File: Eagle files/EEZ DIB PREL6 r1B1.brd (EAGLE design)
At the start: 146 x 95 mm, 66 parts, among them IC1 STM32F030C6T6, IC2 74HC1G126DBVT, IC3 M24C32-WMN6P, IC4 LP2985-33DBVR, K1 RT424005, K2 RT424005, K3 RT424005, K4 RT424005, K5 RT424005, K6 RT424005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

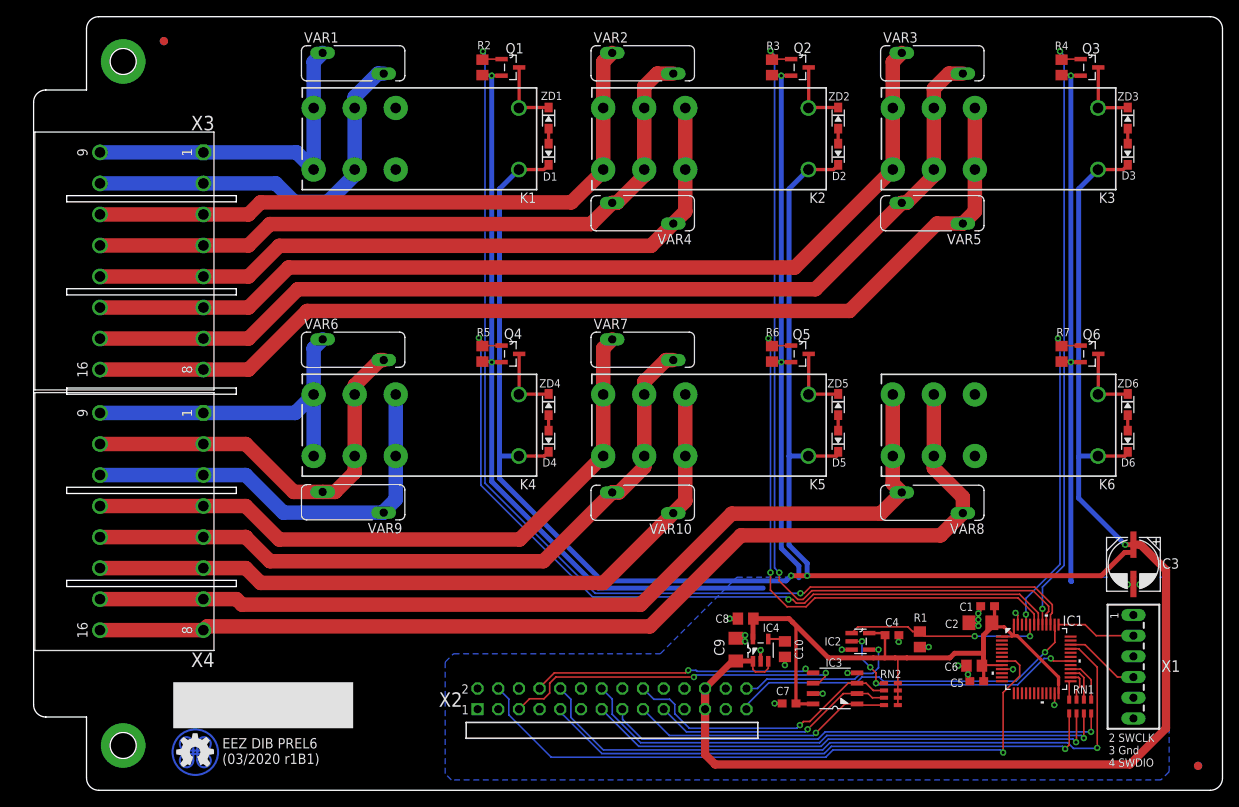
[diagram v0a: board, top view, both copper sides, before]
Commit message: BOM added, improved PCB clearances
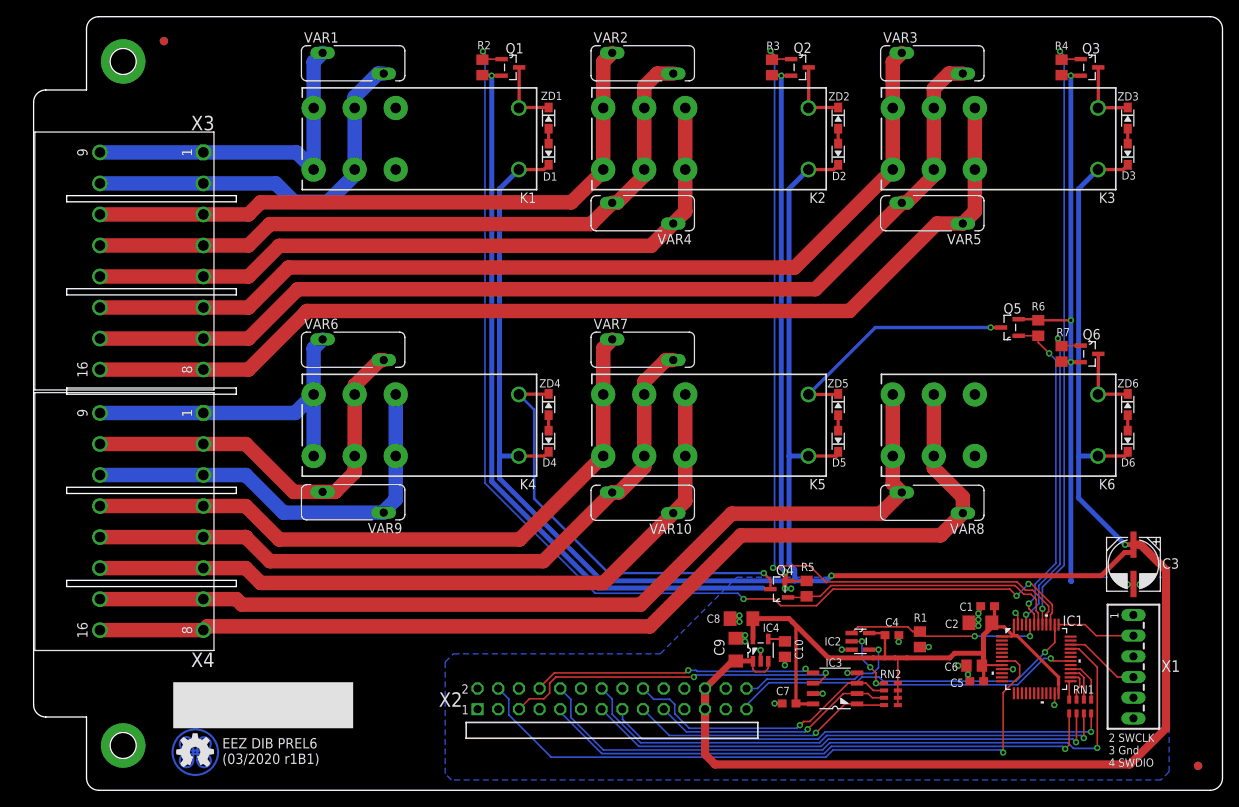
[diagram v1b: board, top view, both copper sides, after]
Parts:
- C8: device rcl:C0805 -> rcl:C1206
- moved R5 49.2 mm to (94.9, 24.8), turned to 90 degrees
- moved Q4 43.9 mm to (91.6, 24.7), turned to 180 degrees
- moved R6 32.9 mm to (123.4, 56.8), turned to 90 degrees
- moved Q5 26.0 mm to (119.9, 56.8), turned to 180 degrees
- moved C8 0.51 mm to (86.9, 21.1)
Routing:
- net PREL3: track 99.0 -> 35.0 mm, vias 2 -> 0
- net N$9: track 8.63 -> 51.5 mm, vias 0 -> 1
- net PREL4: track 70.3 -> 40.4 mm
- net N$11: track 8.63 -> 30.7 mm, vias 0 -> 1
- net GND: track 248.1 -> 253.5 mm, vias 27 -> 30
- net PREL0: track 135.5 -> 137.7 mm, vias 2 -> 4
- net PREL1: track 106.7 -> 105.7 mm
- net +5V: vias 3 -> 2

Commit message: UART relocated
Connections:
- removed net OUT22: IC1.2
- removed net OUT23: IC1.3
- net UART_RX: now also IC1.31; no longer IC1.38
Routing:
- net UART_RX: track 44.2 -> 43.6 mm
- net N$19: track 51.9 -> 52.5 mm
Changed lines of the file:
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@@
 <layer number="25" name="tNames" color="7" fill="1" visible="yes" active="yes"/>
 <layer number="26" name="bNames" color="5" fill="1" visible="no" active="yes"/>
-<layer number="27" name="tValues" color="14" fill="1" visible="yes" active="yes"/>
+<layer number="27" name="tValues" color="14" fill="1" visible="no" active="yes"/>
 <layer number="28" name="bValues" color="10" fill="1" visible="no" active="yes"/>
 <layer number="29" name="tStop" color="7" fill="1" visible="yes" active="yes"/>
@@
 <via x="86.6775" y="20.701" extent="1-16" drill="0.4" shape="square"/>
 </signal>
-<signal name="OUT23">
-<contactref element="IC1" pad="3"/>
-</signal>
-<signal name="OUT22">
-<contactref element="IC1" pad="2"/>
-</signal>
 <signal name="DIB_A0">
 <contactref element="IC3" pad="1"/>
@@
 <contactref element="RN2" pad="1"/>
 <contactref element="IC2" pad="2"/>
-<via x="124.9045" y="16.1925" extent="1-16" drill="0.4" shape="octagon"/>
+<via x="125.095" y="15.875" extent="1-16" drill="0.4" shape="octagon"/>
 <wire x1="104.433" y1="13.161" x2="104.22" y2="13.161" width="0.2032" layer="1"/>
 <via x="102.743" y="15.113" extent="1-16" drill="0.4" shape="octagon"/>
@@
 <wire x1="103.4415" y1="13.1445" x2="103.4415" y2="14.4145" width="0.2032" layer="1"/>
 <wire x1="103.4415" y1="14.4145" x2="102.743" y2="15.113" width="0.2032" layer="1"/>
-<wire x1="127.3429" y1="15.875" x2="125.222" y2="15.875" width="0.2032" layer="1"/>
-<wire x1="125.222" y1="15.875" x2="124.9045" y2="16.1925" width="0.2032" layer="1"/>
-<wire x1="124.9045" y1="16.1925" x2="124.079" y2="16.1925" width="0.2032" layer="16"/>
-<wire x1="124.079" y1="16.1925" x2="120.8405" y2="12.954" width="0.2032" layer="16"/>
-<wire x1="120.8405" y1="12.954" x2="103.632" y2="12.954" width="0.2032" layer="16"/>
+<wire x1="127.3429" y1="15.875" x2="125.095" y2="15.875" width="0.2032" layer="1"/>
+<wire x1="123.825" y1="15.875" x2="120.904" y2="12.954" width="0.2032" layer="16"/>
+<wire x1="120.904" y1="12.954" x2="103.632" y2="12.954" width="0.2032" layer="16"/>
 <wire x1="103.632" y1="12.954" x2="103.4415" y2="13.1445" width="0.2032" layer="16"/>
+<wire x1="125.095" y1="15.875" x2="123.825" y2="15.875" width="0.2032" layer="16"/>
 </signal>
 <signal name="SWDIO">
@@
 </signal>
 <signal name="UART_RX">
-<contactref element="IC1" pad="38"/>
 <contactref element="X2" pad="27"/>
-<wire x1="125.3871" y1="20.3454" x2="125.3871" y2="19.5834" width="0.2032" layer="1"/>
-<wire x1="125.3871" y1="19.5834" x2="125.4125" y2="19.558" width="0.2032" layer="1"/>
-<wire x1="125.4125" y1="19.558" x2="125.4125" y2="18.161" width="0.2032" layer="1"/>
-<via x="124.206" y="16.9545" extent="1-16" drill="0.4" shape="octagon"/>
+<via x="124.587" y="16.891" extent="1-16" drill="0.4" shape="octagon"/>
 <wire x1="87.54" y1="9.96" x2="87.54" y2="10.451" width="0.2032" layer="16"/>
 <wire x1="87.54" y1="10.451" x2="90.297" y2="13.208" width="0.2032" layer="16"/>
@@
 <wire x1="101.0285" y1="13.208" x2="90.297" y2="13.208" width="0.2032" layer="16"/>
 <wire x1="101.727" y1="13.9065" x2="103.8225" y2="13.9065" width="0.2032" layer="16"/>
-<wire x1="125.4125" y1="18.161" x2="124.206" y2="16.9545" width="0.2032" layer="1"/>
 <wire x1="103.8225" y1="13.9065" x2="104.3305" y2="13.3985" width="0.2032" layer="16"/>
-<wire x1="124.206" y1="16.9545" x2="120.65" y2="13.3985" width="0.2032" layer="16"/>
-<wire x1="120.65" y1="13.3985" x2="104.3305" y2="13.3985" width="0.2032" layer="16"/>
+<wire x1="120.7135" y1="13.3985" x2="104.3305" y2="13.3985" width="0.2032" layer="16"/>
+<contactref element="IC1" pad="31"/>
+<wire x1="120.7135" y1="13.3985" x2="124.206" y2="16.891" width="0.2032" layer="16"/>
+<wire x1="124.587" y1="16.891" x2="124.206" y2="16.891" width="0.2032" layer="16"/>
+<wire x1="127.3429" y1="16.383" x2="125.603" y2="16.383" width="0.2032" layer="1"/>
+<wire x1="124.587" y1="16.891" x2="125.095" y2="16.891" width="0.2032" layer="1"/>
+<wire x1="125.095" y1="16.891" x2="125.603" y2="16.383" width="0.2032" layer="1"/>
 </signal>
 <signal name="SWCLK">
@@
 <contactref element="X4" pad="3"/>
 <contactref element="X4" pad="11"/>
-<wire x1="42.993" y1="34.0995" x2="30.6705" y2="34.0995" width="1.778" layer="16"/>
-<wire x1="30.6705" y1="34.0995" x2="26.055" y2="38.715" width="1.778" layer="16"/>
+<wire x1="31.369" y1="33.401" x2="26.055" y2="38.715" width="1.778" layer="16"/>
 <wire x1="20.85" y1="38.715" x2="26.055" y2="38.715" width="1.778" layer="16"/>
 <wire x1="42.993" y1="34.0995" x2="42.993" y2="34.23" width="1.778" layer="16"/>
@@
 <wire x1="44.47" y1="48.611" x2="44.47" y2="41.051" width="1.778" layer="16"/>
 <wire x1="8.15" y1="38.715" x2="20.85" y2="38.715" width="1.778" layer="16"/>
+<wire x1="31.369" y1="33.401" x2="42.2945" y2="33.401" width="1.778" layer="16"/>
+<wire x1="42.2945" y1="33.401" x2="42.993" y2="34.0995" width="1.778" layer="16"/>
 </signal>
 <signal name="N$22">

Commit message: debug connector update
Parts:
- X1: value N.C. -> SSW-106-02-S-S; device EEZ_connectors:22-23-2061 -> con-samtec:SSW-106-02-S-S
- moved X1 2.35 mm to (132.7, 15.2)
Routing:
- net SWCLK: track 9.76 -> 7.41 mm
- net SWDIO: track 9.37 -> 7.02 mm
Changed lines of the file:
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@@
 <rectangle x1="19.6119" y1="7.0038" x2="20.0119" y2="7.0076" layer="21"/>
 <rectangle x1="19.6652" y1="7.0076" x2="19.9052" y2="7.0114" layer="21"/>
-<text x="132.0192" y="6.9627" size="1.016" layer="21" font="vector" ratio="10" rot="SR0" align="top-left">2 SWCLK
+<text x="132.5272" y="6.9627" size="1.016" layer="21" font="vector" ratio="10" rot="SR0" align="top-left">2 SWCLK
 3 Gnd
 4 SWDIO
@@
 <attribute name="VALUE" x="96.3676" y="17.907" size="0.6096" layer="27" ratio="10" rot="SR0"/>
 </element>
-<element name="X1" library="EEZ_connectors" package="22-23-2061" value="N.C." x="135.0645" y="15.1765" smashed="yes" rot="R270">
-<attribute name="OC_NEWARK" value="27C1933" x="135.0645" y="15.1765" size="1.016" layer="27" ratio="10" rot="R270" display="off"/>
-<attribute name="MPN" value="22-23-2061" x="135.0645" y="15.1765" size="1.016" layer="27" ratio="10" rot="R270" display="off"/>
-<attribute name="MF" value="MOLEX" x="135.0645" y="15.1765" size="1.016" layer="27" ratio="10" rot="R270" display="off"/>
-<attribute name="OC_FARNELL" value="1462922" x="135.0645" y="15.1765" size="1.016" layer="27" ratio="10" rot="R270" display="off"/>
-<attribute name="NAME" x="138.4935" y="14.5415" size="1.4224" layer="25" ratio="10"/>
-<attribute name="VALUE" x="132.207" y="18.034" size="1.016" layer="27" ratio="10" rot="R270"/>
-</element>
 <element name="EEZ_SIGNATURE" library="EEZ_Lib1" package="SIGNATURE_5MM" value="SIGNATURESMALL" x="19.8585" y="4.6765" smashed="yes" rot="R180"/>
 <element name="FM2" library="EEZ_Lib1" package="FIDUCIAL_DUAL" value="FIDUCIAL_2" x="143" y="3" smashed="yes"/>
@@
 <attribute name="NAME" x="125.603" y="55.753" size="1.016" layer="25" ratio="10"/>
 <attribute name="VALUE" x="126.238" y="53.594" size="1.016" layer="27" ratio="10" rot="R270" align="center"/>
+</element>
+<element name="X1" library="con-samtec" package="SSW-106-02-S-S" value="SSW-106-02-S-S" x="132.715" y="15.1765" smashed="yes" rot="R270">
+<attribute name="OC_NEWARK" value="11P9416" x="132.715" y="15.1765" size="1.016" layer="27" ratio="10" rot="R270" display="off"/>
+<attribute name="MPN" value="SSW-106-02-S-S" x="132.715" y="15.1765" size="1.016" layer="27" ratio="10" rot="R270" display="off"/>
+<attribute name="MF" value="" x="132.715" y="15.1765" size="1.016" layer="27" ratio="10" rot="R270" display="off"/>
+<attribute name="OC_FARNELL" value="unknown" x="132.715" y="15.1765" size="1.016" layer="27" ratio="10" rot="R270" display="off"/>
+<attribute name="NAME" x="134.3025" y="14.5415" size="1.27" layer="25" ratio="10"/>
+<attribute name="VALUE" x="131.445" y="5.6515" size="1.27" layer="27"/>
 </element>
 </elements>
@@
 <contactref element="C4" pad="2"/>
 <contactref element="IC2" pad="3"/>
-<contactref element="X1" pad="3"/>
 <via x="116.0145" y="20.193" extent="1-16" drill="0.4" shape="square"/>
 <via x="116.0145" y="20.955" extent="1-16" drill="0.4" shape="square"/>
@@
 <wire x1="127.381" y1="57.7215" x2="127.381" y2="52.578" width="0.6096" layer="16"/>
 <via x="86.6775" y="20.701" extent="1-16" drill="0.4" shape="square"/>
+<contactref element="X1" pad="3"/>
 </signal>
 <signal name="DIB_A0">
@@
 <contactref element="IC1" pad="34"/>
 <contactref element="X1" pad="4"/>
-<wire x1="127.3429" y1="17.8816" x2="129.1209" y2="17.8816" width="0.2032" layer="1"/>
-<wire x1="129.1209" y1="17.8816" x2="133.096" y2="13.9065" width="0.2032" layer="1"/>
-<wire x1="135.0645" y1="13.9065" x2="133.096" y2="13.9065" width="0.2032" layer="1"/>
+<wire x1="127.3429" y1="17.8816" x2="128.7399" y2="17.8816" width="0.2032" layer="1"/>
+<wire x1="128.7399" y1="17.8816" x2="132.715" y2="13.9065" width="0.2032" layer="1"/>
 </signal>
 <signal name="UART_RX">
@@
 <signal name="SWCLK">
 <contactref element="IC1" pad="37"/>
-<contactref element="X1" pad="2"/>
 <wire x1="125.8697" y1="20.3454" x2="129.1336" y2="20.3454" width="0.2032" layer="1"/>
 <wire x1="129.1336" y1="20.3454" x2="130.4925" y2="18.9865" width="0.2032" layer="1"/>
-<wire x1="135.0645" y1="18.9865" x2="130.4925" y2="18.9865" width="0.2032" layer="1"/>
+<wire x1="132.715" y1="18.9865" x2="130.4925" y2="18.9865" width="0.2032" layer="1"/>
+<contactref element="X1" pad="2"/>
 </signal>
 <signal name="DIB_NRESET">

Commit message: PCB terminals position adjusted
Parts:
- moved X3 2.20 mm to (12.3, 65.0)
- moved X4 2.20 mm to (12.3, 33.0)
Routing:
- net N$29: track 128.0 -> 130.2 mm
- net N$24: track 82.5 -> 84.7 mm
- net N$22: track 89.9 -> 92.1 mm
- net N$34: track 125.7 -> 127.9 mm
- net N$33: track 119.2 -> 121.4 mm
- net N$32: track 87.9 -> 90.1 mm
- net N$31: track 85.5 -> 87.7 mm
- net N$30: track 79.0 -> 81.2 mm
- net N$28: track 47.9 -> 50.1 mm
- net N$25: track 41.9 -> 44.1 mm
- net N$21: track 42.0 -> 44.2 mm
- net N$19: track 52.5 -> 54.7 mm
- net N$35: track 128.2 -> 130.4 mm
- net N$27: track 116.9 -> 119.1 mm
- net N$26: track 88.0 -> 90.2 mm
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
